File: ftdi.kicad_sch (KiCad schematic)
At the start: 37 parts, among them U2301 NCP718BSN330T1G, U2302 TXU0204BQAR, U2303 FT4232H_VQFN, U2304 TXU0204BQAR, Y2301 Resonator_12MHz_ABM8G

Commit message: [#100282] Update components from library
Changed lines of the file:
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@@
 		(property "MPN" "ABM8G-12.000MHZ-18-D2Y-T"
 			(at 260.35 199.39 0)
-			(hide yes)
 			(show_name no)
 			(do_not_autoplace no)
@@
 	)
 	(symbol
-		(lib_name "R_1M_0402_2")
 		(lib_id "antmicroResistors0402:R_1M_0402")
 		(at 262.89 195.58 0)

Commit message: [#100282] Update selected symbols
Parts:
- D2302: value LED_G_0603_LG_L29K-G2J1-24-Z -> LED_G_0402_VLMTG1500-GS08; footprint antmicro-footprints:LED_0603_1608Metric_G -> antmicro-footprints:LED_0402_1005Metric_G; symbol antmicroLEDIndicationDiscrete:LED_G_0603_LG_L29K-G2J1-24-Z -> antmicroLEDIndicationDiscrete:LED_G_0402_VLMTG1500-GS08; MPN LG L29K-G2J1-24-Z -> VLMTG1500-GS08; Manufacturer OSRAM -> Vishay
- U2302, U2304: value TXU0204BQAR -> TXU0304BQAR
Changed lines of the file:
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@@
 	)
 	(symbol
-		(lib_id "antmicroLEDIndicationDiscrete:LED_G_0603_LG_L29K-G2J1-24-Z")
+		(lib_id "antmicroLEDIndicationDiscrete:LED_G_0402_VLMTG1500-GS08")
 		(at 247.65 78.74 270)
 		(mirror x)
@@
 		(in_pos_files yes)
 		(dnp no)
+		(fields_autoplaced yes)
 		(property "Reference" "D2302"
-			(at 246.38 74.93 90)
+			(at 245.11 74.93 90)
 			(show_name no)
 			(do_not_autoplace no)
@@
 			)
 		)
-		(property "Value" "LED_G_0603_LG_L29K-G2J1-24-Z"
-			(at 240.03 58.42 0)
+		(property "Value" "LED_G_0402_VLMTG1500-GS08"
+			(at 240.03 55.88 0)
 			(hide yes)
 			(show_name no)
@@
 			)
 		)
-		(property "Footprint" "antmicro-footprints:LED_0603_1608Metric_G"
-			(at 237.49 58.42 0)
+		(property "Footprint" "antmicro-footprints:LED_0402_1005Metric_G"
+			(at 237.49 55.88 0)
 			(hide yes)
 			(show_name no)
@@
 			)
 		)
-		(property "Datasheet" "https://look.ams-osram.com/m/19ee86b3ae0ee95b/original/LG-L29K.pdf"
-			(at 234.95 58.42 0)
+		(property "Datasheet" "https://www.vishay.com/docs/82554/vlmo1500.pdf"
+			(at 234.95 55.88 0)
 			(hide yes)
 			(show_name no)
@@
 			)
 		)
-		(property "Description" "LED, Green, SMD, 0603, 20 mA, 1.7 V, 570 nm"
-			(at 222.25 58.42 0)
+		(property "Description" "LED, Green, SMD, 1005, 5 mA, 3.1 V, 535 nm"
+			(at 222.25 55.88 0)
 			(hide yes)
 			(show_name no)
@@
 			)
 		)
-		(property "MPN" "LG L29K-G2J1-24-Z"
-			(at 232.41 58.42 0)
+		(property "MPN" "VLMTG1500-GS08"
+			(at 232.41 55.88 0)
 			(hide yes)
 			(show_name no)
@@
 			)
 		)
-		(property "Manufacturer" "OSRAM"
-			(at 229.87 58.42 0)
+		(property "Manufacturer" "Vishay"
+			(at 229.87 55.88 0)
 			(hide yes)
 			(show_name no)
@@
 		)
 		(property "Color" "Green"
-			(at 246.38 77.4699 90)
+			(at 245.11 77.4699 90)
 			(show_name no)
 			(do_not_autoplace no)
@@
 		)
 		(property "Author" "Antmicro"
-			(at 227.33 58.42 0)
+			(at 227.33 55.88 0)
 			(hide yes)
 			(show_name no)
@@
 		)
 		(property "License" "Apache-2.0"
-			(at 224.79 58.42 0)
+			(at 224.79 55.88 0)
 			(hide yes)
 			(show_name no)
@@
 			)
 		)
-		(property "Value" "TXU0204BQAR"
+		(property "Value" "TXU0304BQAR"
 			(at 116.84 158.75 0)
 			(hide yes)
@@
 			)
 		)
-		(property "Value" "TXU0204BQAR"
+		(property "Value" "TXU0304BQAR"
 			(at 116.84 97.79 0)
 			(hide yes)

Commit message: [#100282] Clear ERC
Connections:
- net +1V8: no longer C2309.2, C2310.2, C2311.2, C2312.2, U2303.2 (V_{CORE}), U2303.31 (V_{CORE}), U2303.43 (V_{REGOUT})
- new net +1V8_FTDI: C2309.2, C2310.2, C2311.2, C2312.2, U2303.2 (V_{CORE}), U2303.31 (V_{CORE}), U2303.43 (V_{REGOUT})
- no-connect marks 34 -> 35
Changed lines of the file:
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@@
+	)
+	(no_connect
+		(at 194.31 162.56)
 	)
 	(no_connect
@@
 		)
 	)
-	(label "+1V8"
+	(label "+1V8_FTDI"
 		(at 273.05 107.95 180)
 		(effects

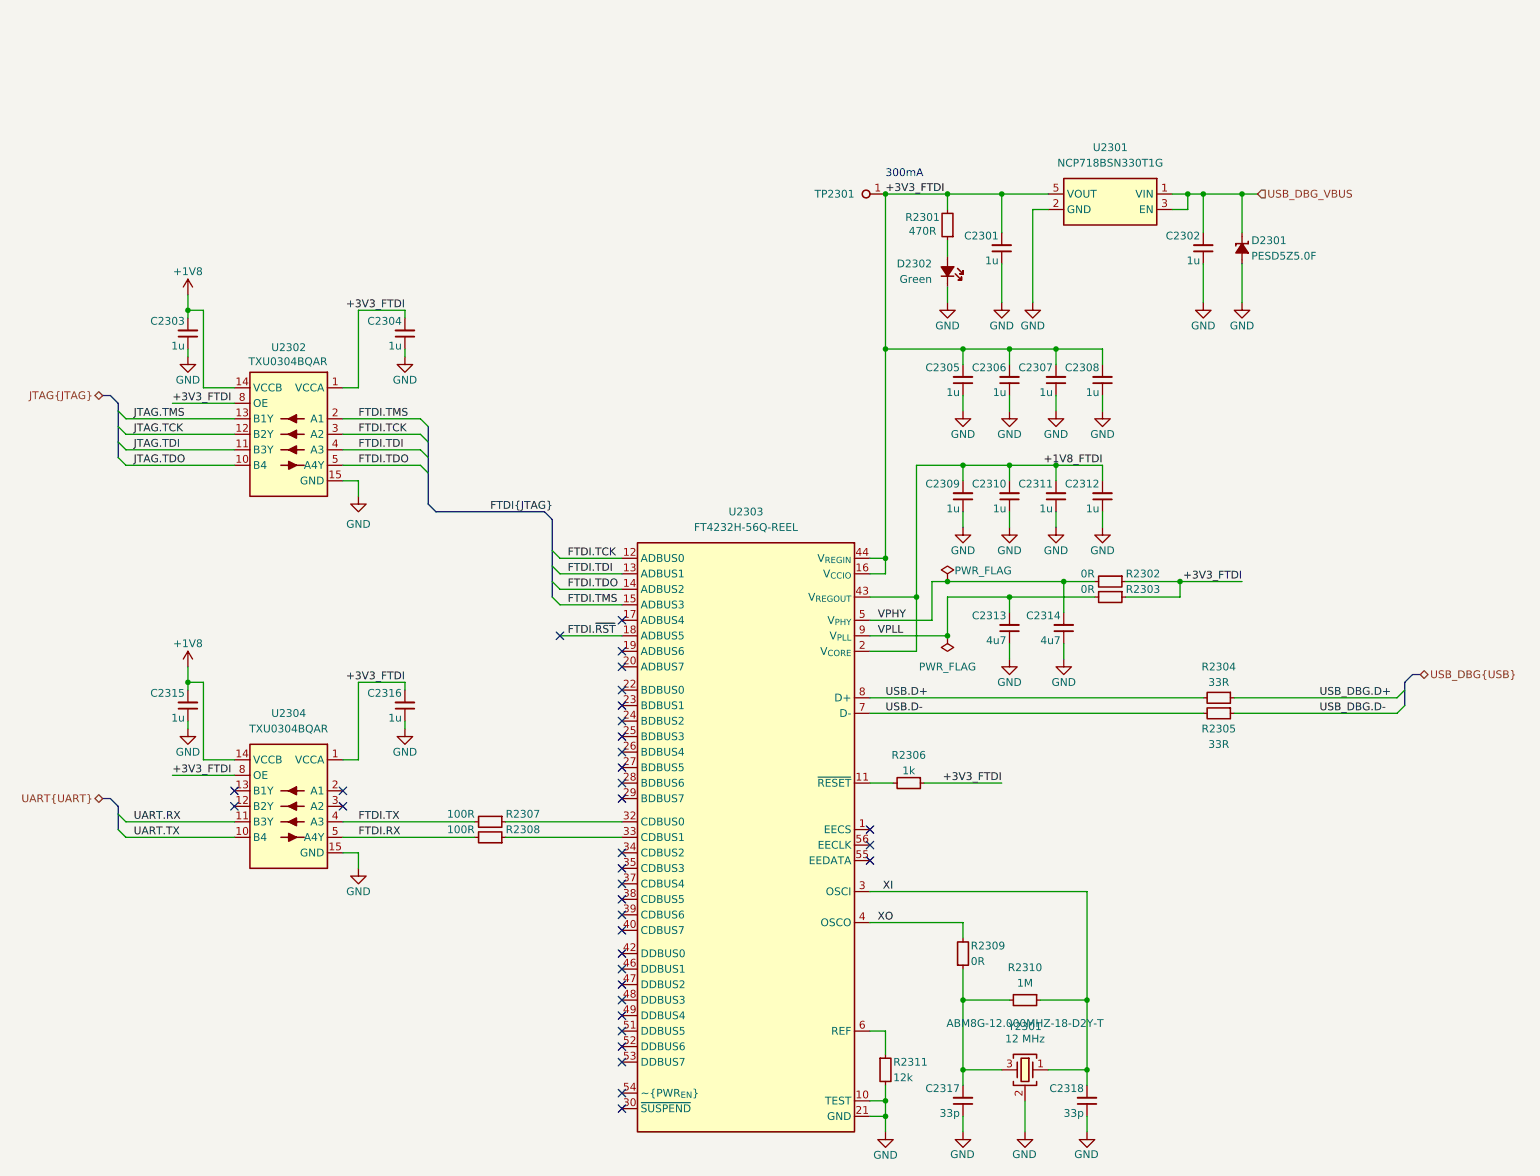
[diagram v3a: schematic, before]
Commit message: [#100282] Fix overlaping graphics, add schematic sheet names on them
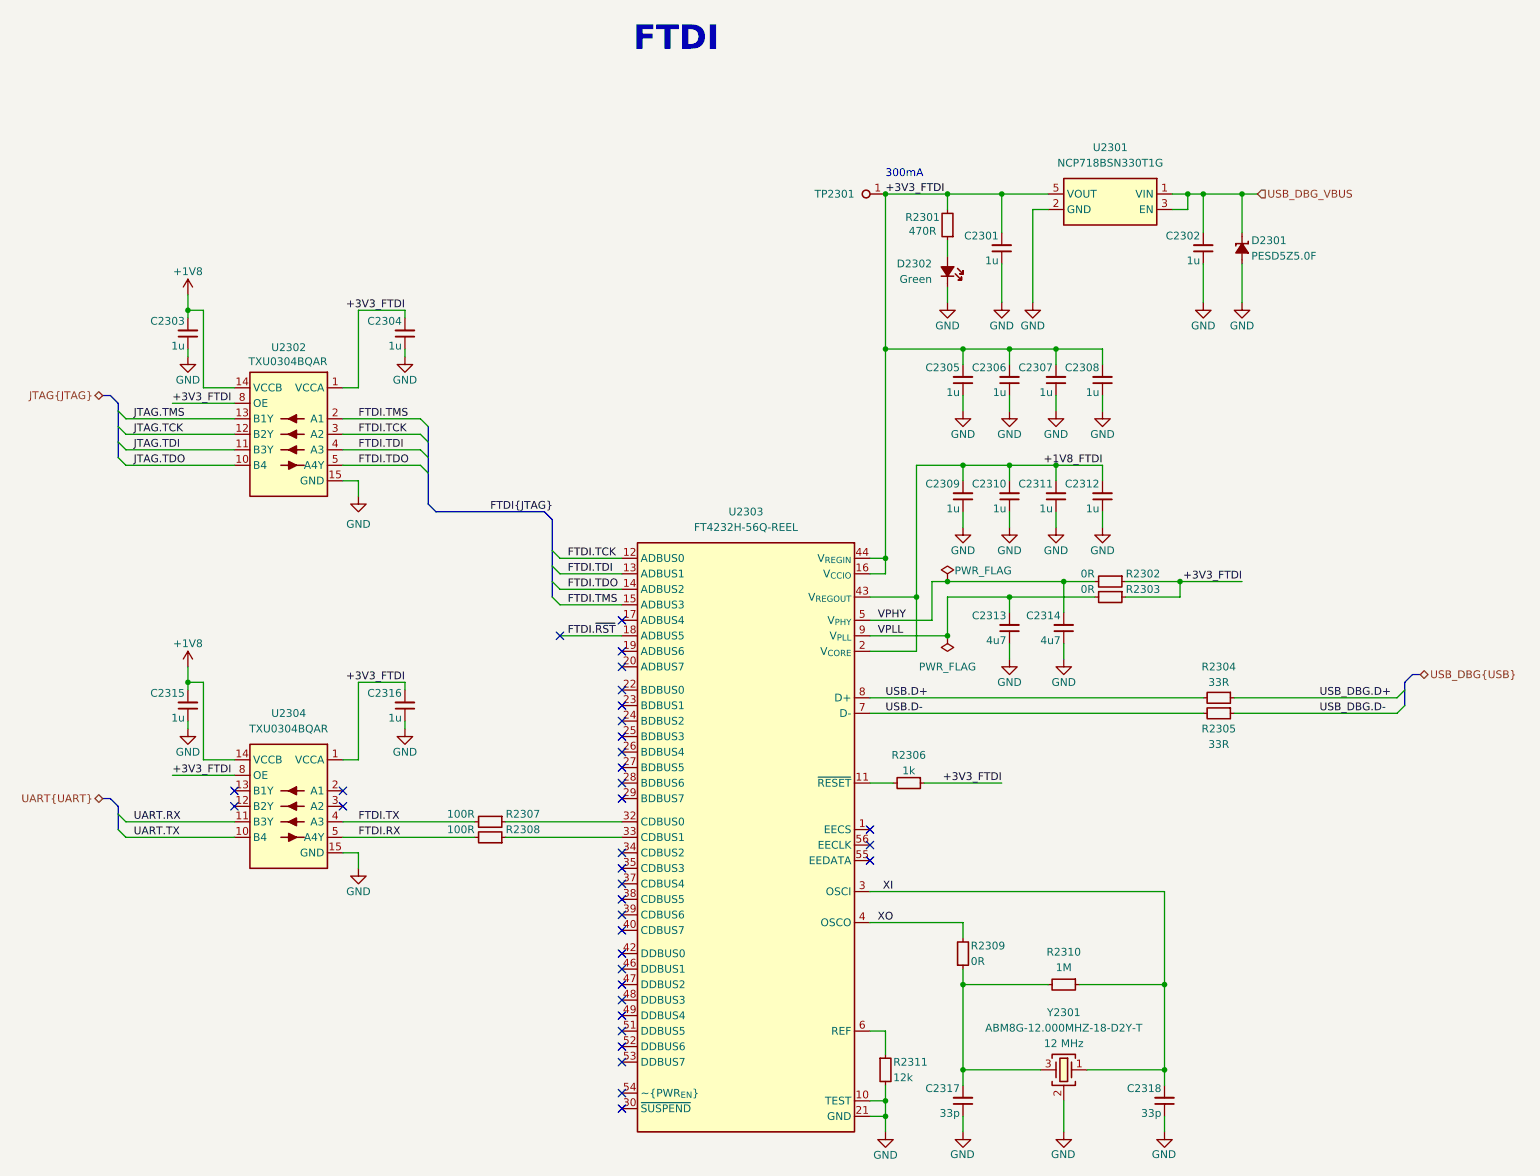
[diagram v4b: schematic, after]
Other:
- note added: "FTDI"
- moved on the sheet: C2318, R2310, Y2301
